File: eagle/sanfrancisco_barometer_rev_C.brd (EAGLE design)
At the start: 72 x 42 mm, 39 parts, among them IC1 PIC18F2580, IC2 MPL115A1, IC3 MCP2551SN, IC4 LM2575S, IC5 LM2931M, J2 A00-108-220-450, Q1 10 MHz

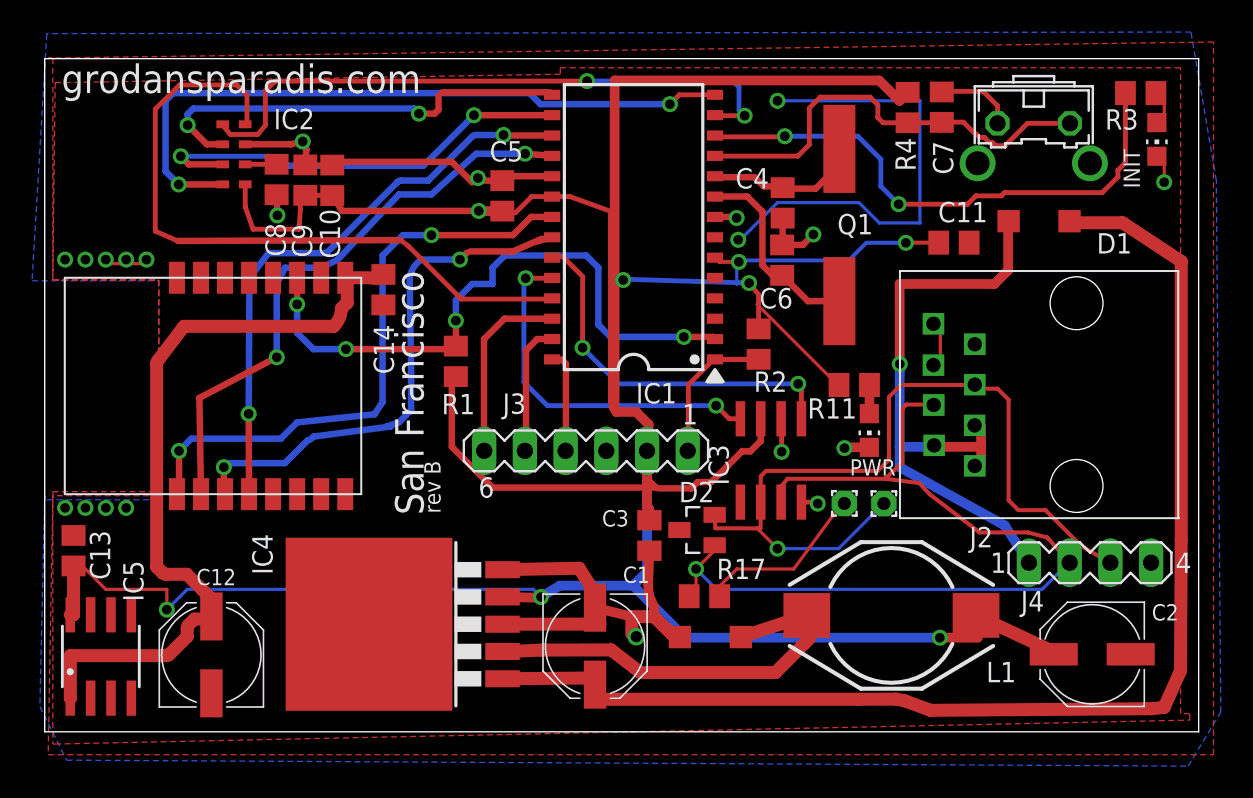
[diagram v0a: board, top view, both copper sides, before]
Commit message: Changed component symbols
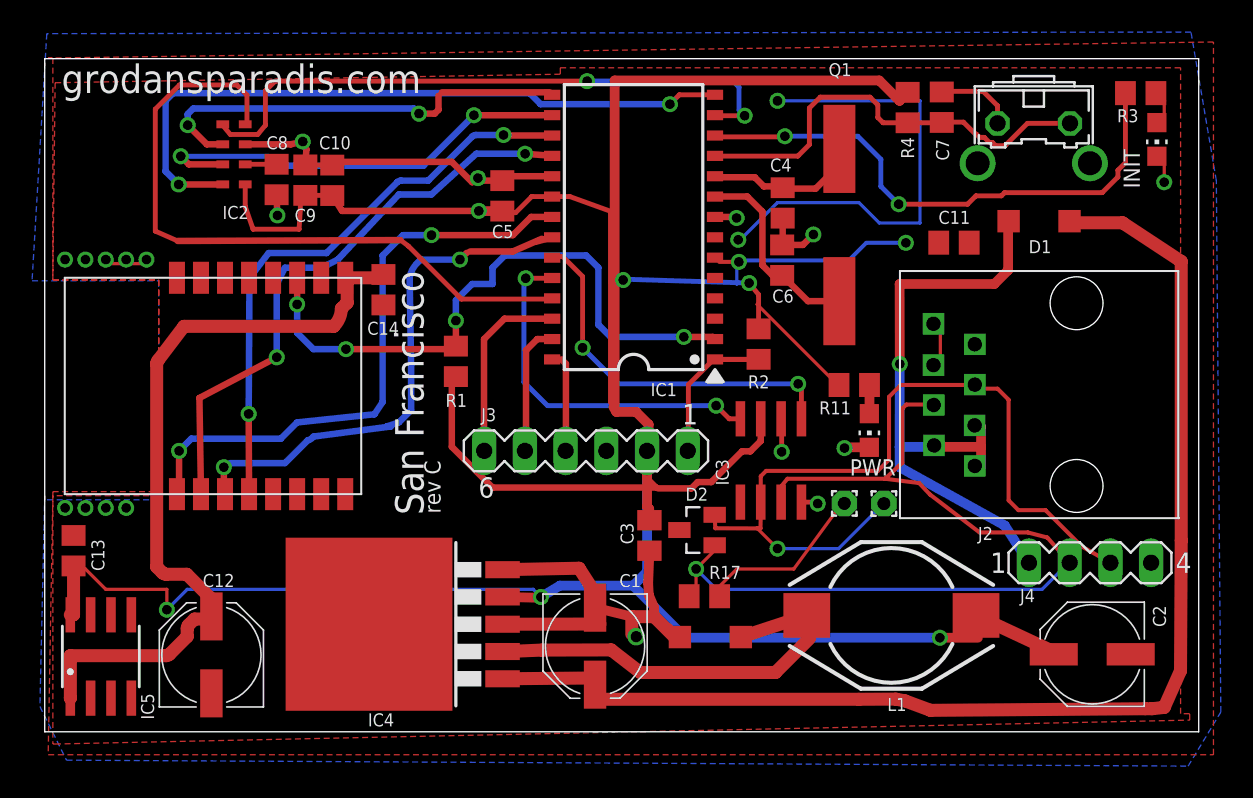
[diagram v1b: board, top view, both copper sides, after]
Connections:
- new net N$8: C11.2, IC1.6
- net VCC: no longer C11.2, IC1.6
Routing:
- net VCC: track 234.2 -> 231.8 mm
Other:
- board text added: "rev C"
- board text removed: "rev B"
